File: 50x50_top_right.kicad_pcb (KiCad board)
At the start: 2 copper layers, 48.9 x 48.3 mm, 102 parts, among them CON1 BARREL_JACK, J1 INTERCONNECT_1X03, J10 INTERCONNECT_1X03, J11 INTERCONNECT_1X03, J12 INTERCONNECT_1X03, J13 INTERCONNECT_1X03, J14 INTERCONNECT_1X03, J15 INTERCONNECT_1X03, J16 INTERCONNECT_1X03, J17 INTERCONNECT_1X03, J18 INTERCONNECT_1X03, J19 INTERCONNECT_1X03, J2 INTERCONNECT_1X03, J20 INTERCONNECT_1X03, J21 INTERCONNECT_1X03, J22 INTERCONNECT_1X03, J23 INTERCONNECT_1X03, J24 INTERCONNECT_1X03, J25 INTERCONNECT_1X03, J26 INTERCONNECT_1X03, J27 INTERCONNECT_1X03, J28 INTERCONNECT_1X03, J29 INTERCONNECT_1X03, J3 INTERCONNECT_1X03, J30 INTERCONNECT_1X03, J31 INTERCONNECT_1X03, J32 INTERCONNECT_1X03, J33 INTERCONNECT_1X03, J34 INTERCONNECT_1X03, J35 INTERCONNECT_1X03, J36 INTERCONNECT_1X03, J37 INTERCONNECT_1X03, J38 INTERCONNECT_1X03, J39 INTERCONNECT_1X03, J4 INTERCONNECT_1X03, J40 INTERCONNECT_1X03, J41 INTERCONNECT_1X03, J42 INTERCONNECT_1X03, J43 INTERCONNECT_1X03, J44 INTERCONNECT_1X03, J45 INTERCONNECT_1X03, J46 INTERCONNECT_1X03, J47 INTERCONNECT_1X03, J48 INTERCONNECT_1X03, J49 INTERCONNECT_1X03, J5 INTERCONNECT_1X03, J50 INTERCONNECT_1X03, J51 INTERCONNECT_1X03, J52 INTERCONNECT_1X03, J53 INTERCONNECT_1X03, J54 INTERCONNECT_1X03, J55 INTERCONNECT_1X03, J56 INTERCONNECT_1X03, J57 INTERCONNECT_1X03, J58 INTERCONNECT_1X03, J59 INTERCONNECT_1X03, J6 INTERCONNECT_1X03, J60 INTERCONNECT_1X03, J61 INTERCONNECT_1X03, J62 INTERCONNECT_1X03, J63 INTERCONNECT_1X03, J64 INTERCONNECT_1X03, J65 INTERCONNECT_1X02, J7 INTERCONNECT_1X03, J8 INTERCONNECT_1X03, J9 INTERCONNECT_1X03, P1 CONN_6X2, P2 CONN_6X2, U1 LM7805CT

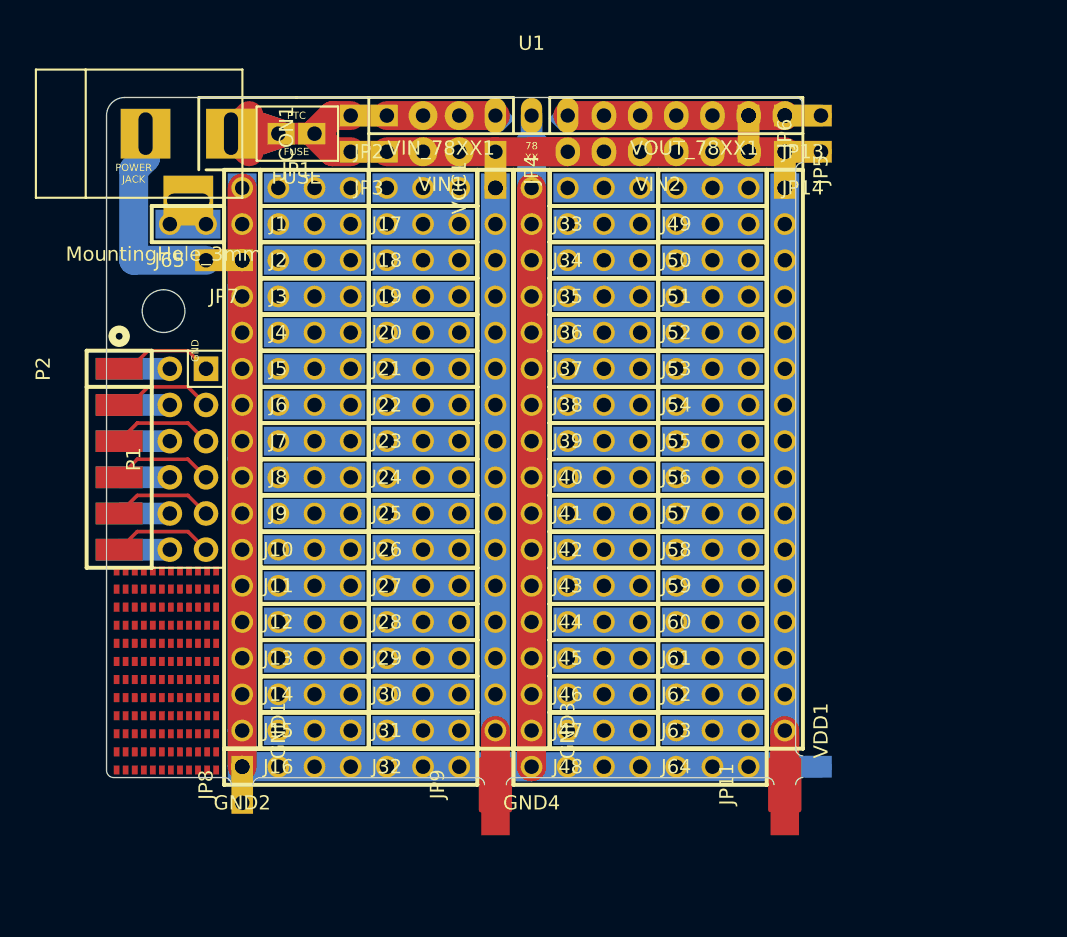
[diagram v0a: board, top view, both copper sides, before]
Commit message: flipped top-right corner and fixed its consequences
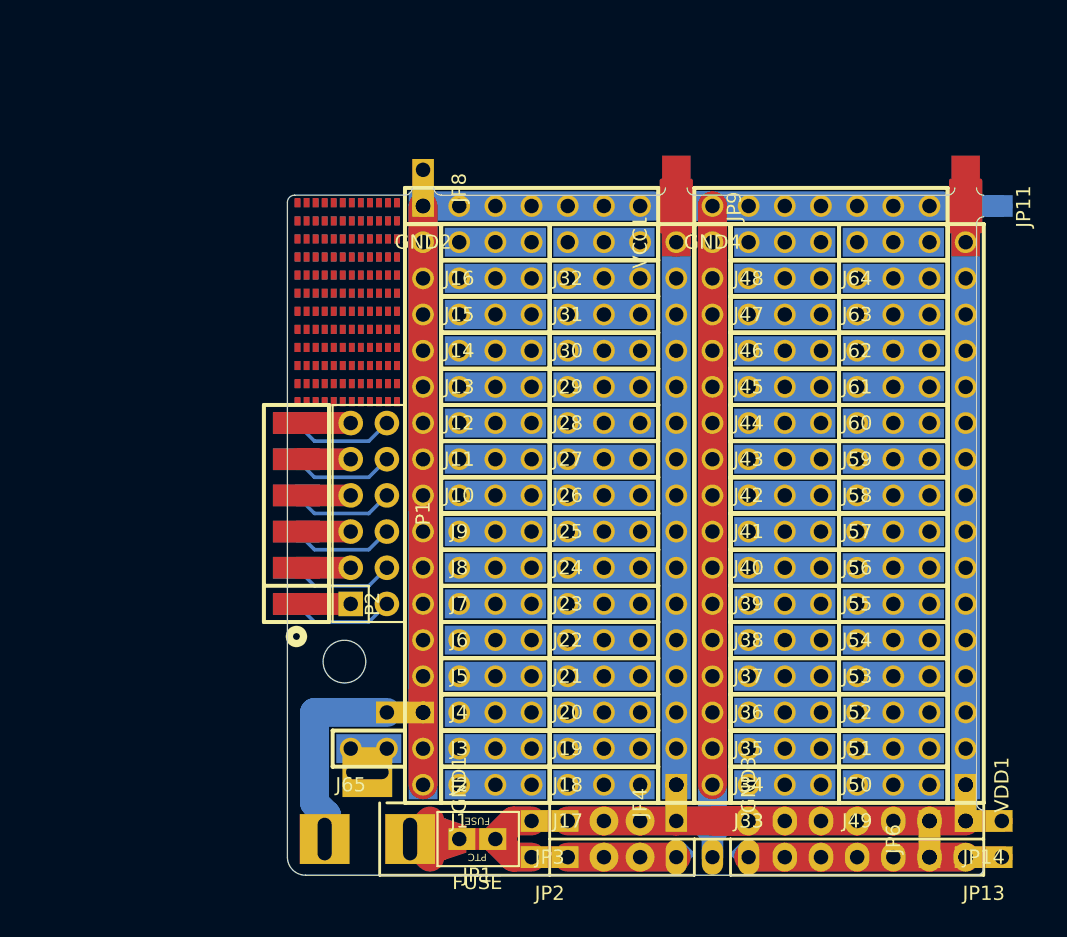
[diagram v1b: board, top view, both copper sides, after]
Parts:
- removed the Ref** at (33.4, 68.2)
- removed the Ref** at (33.4, 63.1)
- removed the Ref** at (33.4, 58.0)
- added Ref**: Val**, SMD:SMD_127_065_grid_4X12, F.Cu at (46.1, 32.2)
- added Ref**: Val**, SMD:SMD_127_065_grid_4X12, F.Cu at (46.1, 37.2)
- added Ref**: Val**, SMD:SMD_127_065_grid_4X12, F.Cu at (46.1, 42.3)
- added Ref**: Val**, SMD:SMD_127_065_grid_4X12, B.Cu at (46.1, 32.2)
- added Ref**: Val**, SMD:SMD_127_065_grid_4X12, B.Cu at (46.1, 37.2)
- added Ref**: Val**, SMD:SMD_127_065_grid_4X12, B.Cu at (46.1, 42.3)
- CON1, F1, JP5, JP7, MountingHole_3mm, U1, VIN1, VIN2, VIN_78XX1, VOUT_78XX1: moved to B.Cu
- F2: moved to F.Cu
- moved JP13 53.6 mm to (91.4, 76.2)
- moved JP2 53.6 mm to (61.0, 76.2)
- moved U1 53.6 mm to (72.4, 76.2)
- moved VIN_78XX1 53.6 mm to (66.0, 76.2)
- moved VOUT_78XX1 53.6 mm to (83.8, 76.2)
- moved C2 51.6 mm to (73.7, 75.2), turned to 135 degrees
- moved C1 51.6 mm to (71.1, 75.2), turned to 45 degrees
- moved F1 51.1 mm to (55.9, 74.9)
- moved F2 51.1 mm to (55.9, 74.9)
- moved JP1 51.1 mm to (55.9, 74.9)
- moved JP6 51.1 mm to (87.6, 74.9), turned to 270 degrees
- moved CON1 51.1 mm to (45.0, 74.9)
- moved JP14 48.7 mm to (91.4, 73.7)
- moved JP3 48.7 mm to (61.0, 73.7)
- moved VIN1 48.7 mm to (66.0, 73.7)
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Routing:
- net Net-(C1-Pad2): track 220.1 -> 230.3 mm
- net Net-(P1-Pad8): track 3.56 -> 7.40 mm
- net Net-(P1-Pad12): track 3.56 -> 7.40 mm
- net Net-(P1-Pad10): track 3.56 -> 7.40 mm
- net Net-(P1-Pad6): track 3.56 -> 7.40 mm
- net Net-(P1-Pad4): track 3.56 -> 7.40 mm
- net Net-(P1-Pad2): track 3.56 -> 7.40 mm
- net Net-(P1-Pad9): track 7.15 -> 3.81 mm
- net Net-(P1-Pad7): track 7.15 -> 3.81 mm
- net Net-(P1-Pad5): track 7.15 -> 3.81 mm
- net Net-(P1-Pad3): track 7.15 -> 3.81 mm
- net Net-(P1-Pad11): track 7.15 -> 3.81 mm
- net Net-(P1-Pad1): track 7.15 -> 3.81 mm
- net Net-(JP11-Pad1): track 2.54 -> 0.00 mm
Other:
- outline, holes or cut-outs redrawn
- board text removed: "GND"
- board text removed: "VCC"

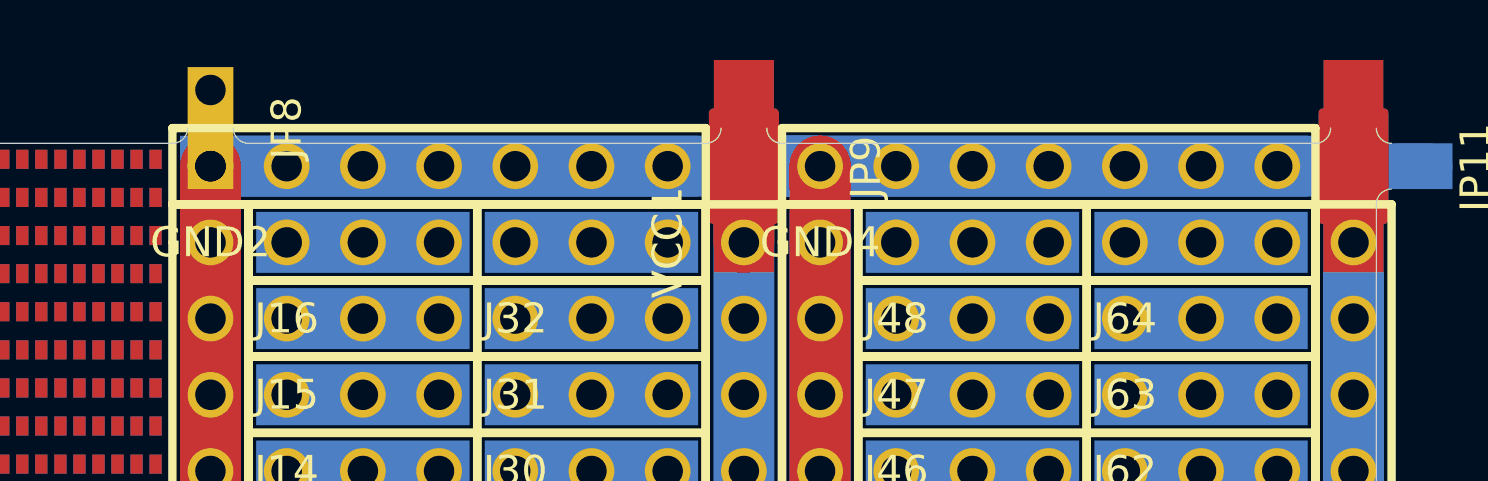
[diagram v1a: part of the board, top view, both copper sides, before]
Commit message: fixed exposed frontside copper for GND traces
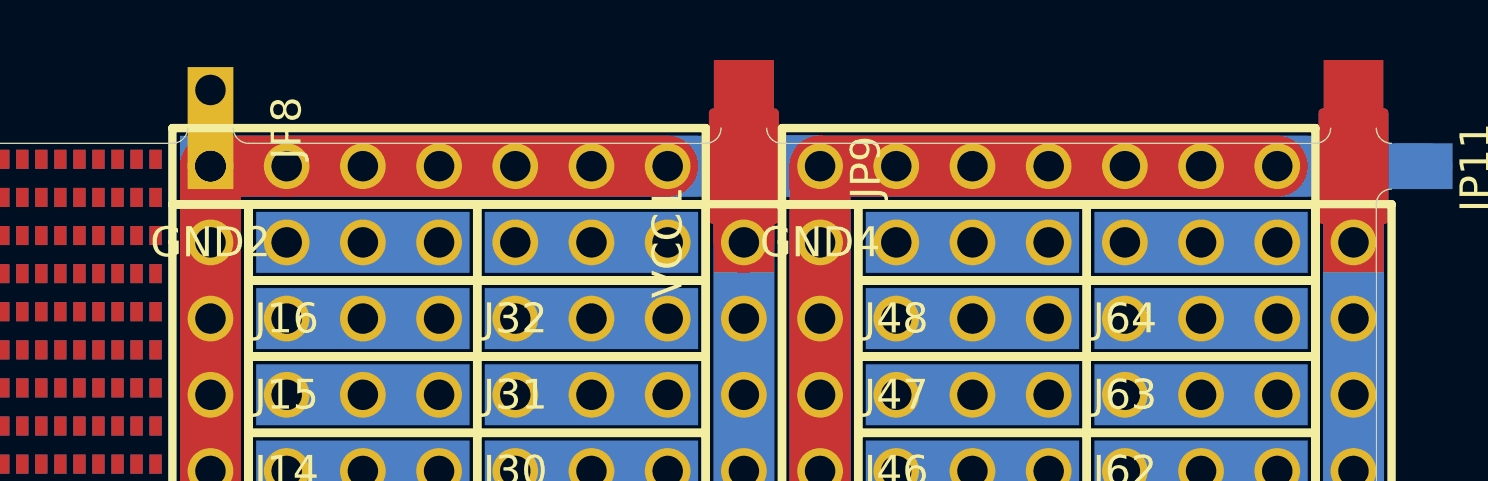
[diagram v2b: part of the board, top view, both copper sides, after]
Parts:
- removed the Ref** at (46.1, 32.2) (x2)
- removed the Ref** at (46.1, 37.2) (x2)
- removed the Ref** at (46.1, 42.3) (x2)
- added Ref**: Val**, SMD:SMD_127_065_grid_4X12, F.Cu at (46.1, 32.2)
- added Ref**: Val**, SMD:SMD_127_065_grid_4X12, F.Cu at (46.1, 37.2)
- added Ref**: Val**, SMD:SMD_127_065_grid_4X12, F.Cu at (46.1, 42.3)
- added Ref**: Val**, SMD:SMD_127_065_grid_4X12, B.Cu at (46.1, 32.2)
- added Ref**: Val**, SMD:SMD_127_065_grid_4X12, B.Cu at (46.1, 37.2)
- added Ref**: Val**, SMD:SMD_127_065_grid_4X12, B.Cu at (46.1, 42.3)
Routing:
- net Net-(C1-Pad2): track 230.3 -> 260.7 mm

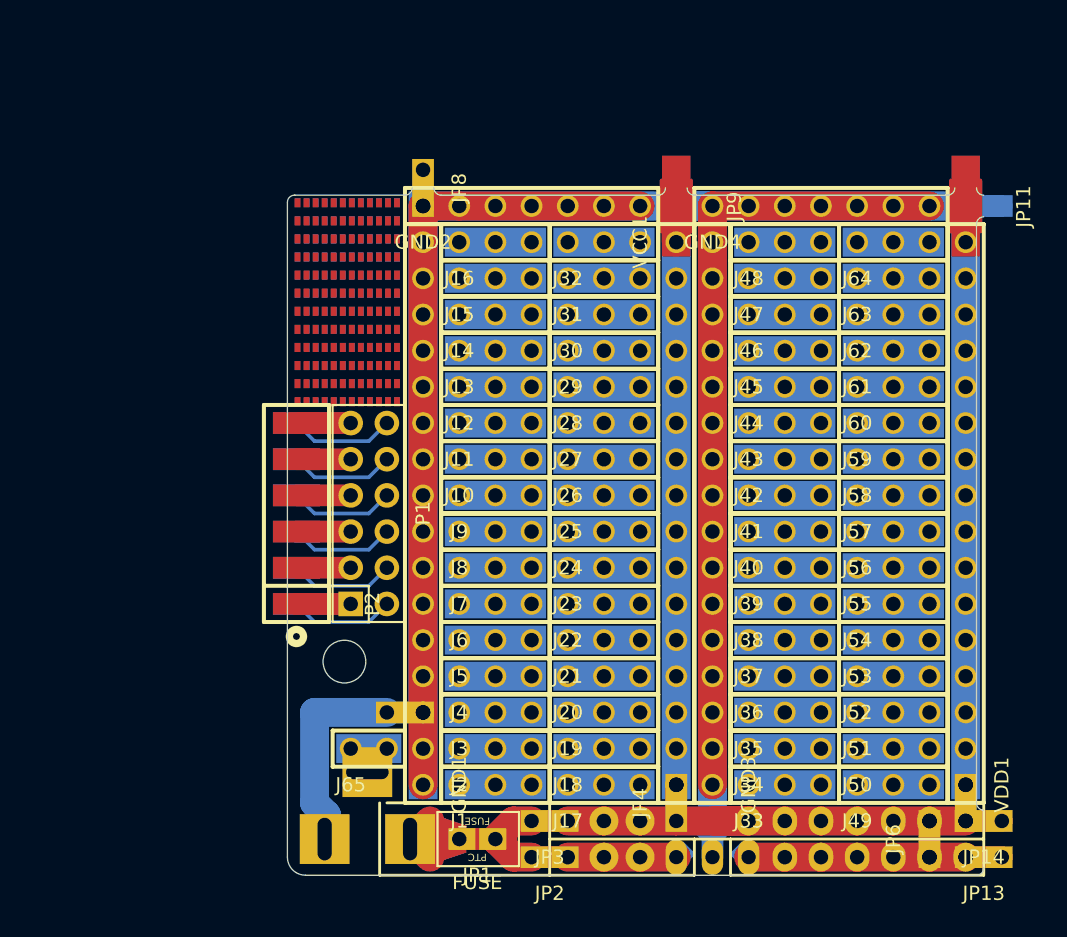
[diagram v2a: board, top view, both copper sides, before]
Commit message: moved shorted inter-board GND connection to center, switched av from Oddities:NetTie-I_Connected_SMD because they were asymmetrical and fixed pin header outlines
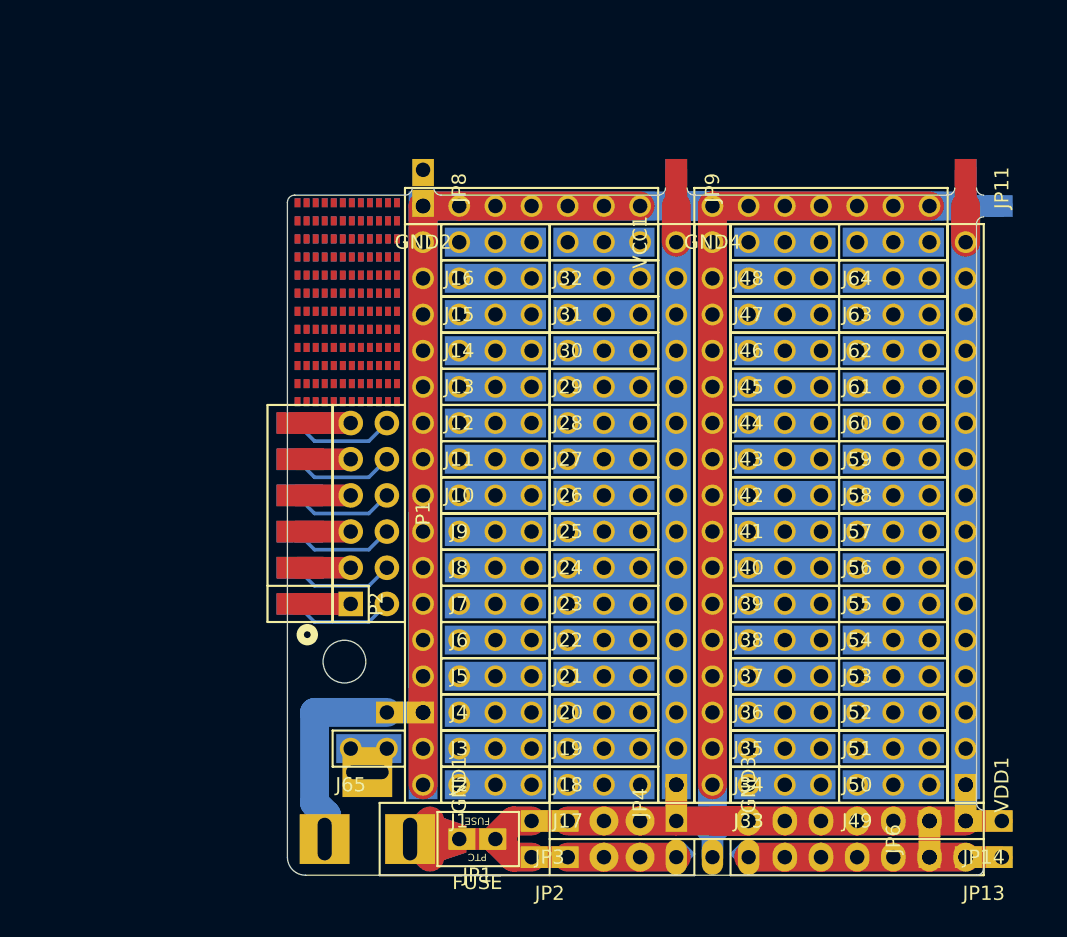
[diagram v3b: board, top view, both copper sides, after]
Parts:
- JP10: footprint 2.54mm_Pin_Headers:Solder_Jumper_SMD_1x2 -> 2.54mm_Pin_Headers:Solder_Jumper_SMD_1x2_Shorted
- JP11, JP9: footprint Oddities:NetTie-I_Connected_SMD -> 2.54mm_Pin_Headers:Solder_Jumper_SMD_1x2_Shorted
- JP15: footprint 2.54mm_Pin_Headers:Solder_Jumper_SMD_1x2_Shorted -> 2.54mm_Pin_Headers:Solder_Jumper_SMD_1x2
- moved JP11 1.27 mm to (90.2, 29.2)
- moved JP9 1.27 mm to (69.8, 29.2)
- moved P2 0.25 mm to (43.4, 58.4)
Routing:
- net Net-(JP11-Pad1): track 0.00 -> 2.54 mm
